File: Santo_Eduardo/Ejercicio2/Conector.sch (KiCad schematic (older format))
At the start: 6 parts, among them U1 AMIS42665TJAA1RG

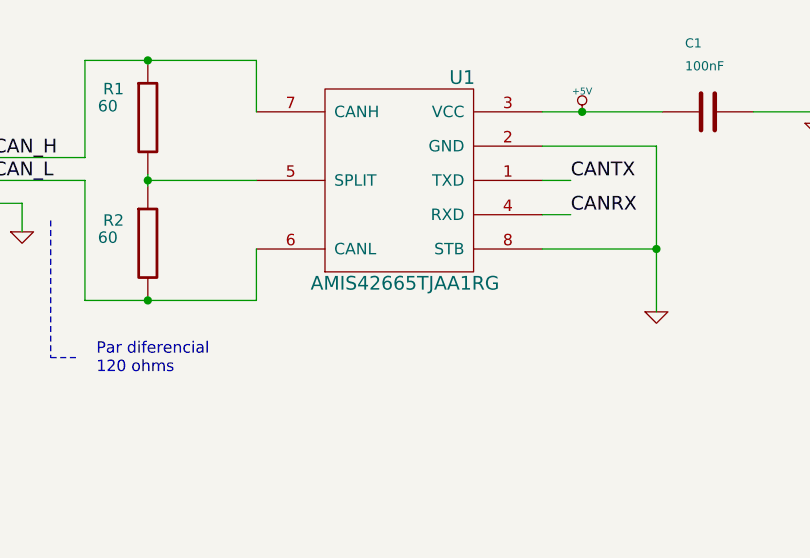
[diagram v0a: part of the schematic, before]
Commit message: Realizado el Electrical Rule Check. Corregidos Errores Se agregó campo Digikey/Mouser en todos los componentes Se modificó Digikey/Mouser en U1 y U2
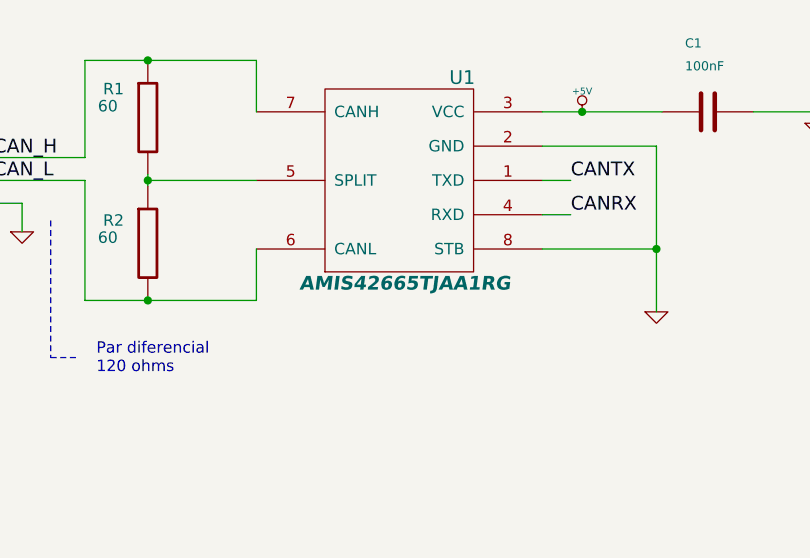
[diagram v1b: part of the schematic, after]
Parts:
- U1: Digikey/Mouser (none) -> 766-1006-1-ND
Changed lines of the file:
@@
 P 8350 4200
 F 0 "U1" H 8100 4700 60  0000 C CNN
-F 1 "AMIS42665TJAA1RG" H 8350 3800 60  0000 C CNN
+F 1 "AMIS42665TJAA1RG" H 8350 3800 60  0000 C CIB
 F 2 "" H 8350 4250 60  0000 C CNN
 F 3 "" H 8350 4250 60  0000 C CNN
+F 4 "766-1006-1-ND" H 8350 4200 60  0001 C CNN "Digikey/Mouser"
 	1    8350 4200
 	-1   0    0    -1

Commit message: Added footprint library Assigned Foot-Symbol updated netlist and BOM
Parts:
- C1: footprint (none) -> Ejercicio2:C_0603_HandSoldering
- JP1: footprint (none) -> Ejercicio2:CON_PALETA_3
- R1, R2: footprint (none) -> Ejercicio2:R_1206_HandSoldering
- U1: footprint (none) -> Ejercicio2:SOIC-8
- XA1: footprint (none) -> Ejercicio2:Conn_Poncho_Derecha
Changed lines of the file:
@@
 F 0 "XA1" H 4125 3925 60  0000 C CNN
 F 1 "Conn_Poncho2P_2x_20x2" H 4175 1825 60  0000 C CNN
-F 2 "" H 3825 3525 60  0000 C CNN
+F 2 "Ejercicio2:Conn_Poncho_Derecha" H 3825 3525 60  0001 C CNN
 F 3 "" H 3825 3525 60  0000 C CNN
 	1    3825 3525
@@
 F 0 "U1" H 8100 4700 60  0000 C CNN
 F 1 "AMIS42665TJAA1RG" H 8350 3800 60  0000 C CIB
-F 2 "" H 8350 4250 60  0000 C CNN
+F 2 "Ejercicio2:SOIC-8" H 8350 4250 60  0001 C CNN
 F 3 "" H 8350 4250 60  0000 C CNN
 F 4 "766-1006-1-ND" H 8350 4200 60  0001 C CNN "Digikey/Mouser"
@@
 F 0 "C1" V 9375 3750 40  0000 L CNN
 F 1 "100nF" V 9475 3750 40  0000 L CNN
-F 2 "" H 9713 3700 30  0000 C CNN
+F 2 "Ejercicio2:C_0603_HandSoldering" H 9713 3700 30  0001 C CNN
 F 3 "" H 9675 3850 60  0000 C CNN
 	1    9675 3850
@@
 F 0 "R1" H 7075 4000 50  0000 C CNN
 F 1 "60" H 7050 3925 50  0000 C CNN
-F 2 "" H 7225 3875 60  0000 C CNN
+F 2 "Ejercicio2:R_1206_HandSoldering" H 7225 3875 60  0001 C CNN
 F 3 "" H 7225 3875 60  0000 C CNN
 	1    7225 3875
@@
 F 0 "R2" H 7075 4525 50  0000 C CNN
 F 1 "60" H 7050 4450 50  0000 C CNN
-F 2 "" H 7225 4425 60  0000 C CNN
+F 2 "Ejercicio2:R_1206_HandSoldering" H 7225 4425 60  0001 C CNN
 F 3 "" H 7225 4425 60  0000 C CNN
 	1    7225 4425
@@
 F 0 "JP1" H 6250 3900 60  0000 C CNN
 F 1 "CONN_3" H 6300 3400 60  0000 C CNN
-F 2 "" H 6200 3900 60  0000 C CNN
+F 2 "Ejercicio2:CON_PALETA_3" H 6200 3900 60  0001 C CNN
 F 3 "" H 6200 3900 60  0000 C CNN
 	1    6200 3900

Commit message: Cambiados footprints Revisando placement en PCB
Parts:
- C1: footprint Ejercicio2:C_0603_HandSoldering -> Ejercicio2:1206
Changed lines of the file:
@@
 F 0 "C1" V 9375 3750 40  0000 L CNN
 F 1 "100nF" V 9475 3750 40  0000 L CNN
-F 2 "Ejercicio2:C_0603_HandSoldering" H 9713 3700 30  0001 C CNN
+F 2 "Ejercicio2:1206" H 9713 3700 30  0001 C CNN
 F 3 "" H 9675 3850 60  0000 C CNN
 	1    9675 3850

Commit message: Probada característica lenght tunning.
Falló Kicad y no pude realizar el par diferencial
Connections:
- net CAN_H renamed CAN_P
- net CAN_L renamed CAN_N
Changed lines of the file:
@@
 	8950 4150 9075 4150
 Text Label 6550 4050 0    60   ~ 0
-CAN_H
+CAN_P
 Text Label 6550 4150 0    60   ~ 0
-CAN_L
+CAN_N
 Wire Wire Line
 	6400 4050 6950 4050
